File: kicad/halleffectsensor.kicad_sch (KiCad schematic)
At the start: 22 parts, among them J1 Conn_01x03, J2 Conn_01x02, Q1 2N3904, U3 ER_OLEDM0.91_1x-I2C, U5 XIAO-nRF52840-SMD

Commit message: Finished PCB and BOM
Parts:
- U2: footprint Package_SO:SOIC-8_4.4x5.0mm_P1.27mm -> Package_SO:JEITA_SOIC-8_3.9x4.9mm_P1.27mm
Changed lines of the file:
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@@
 			)
 		)
-		(property "Footprint" "Package_SO:SOIC-8_4.4x5.0mm_P1.27mm"
+		(property "Footprint" "Package_SO:JEITA_SOIC-8_3.9x4.9mm_P1.27mm"
 			(at 97.79 48.26 0)
 			(hide yes)
@@
 			)
 		)
-		(property "Footprint" "Package_SO:SOIC-8_4.4x5.0mm_P1.27mm"
+		(property "Footprint" "Package_SO:JEITA_SOIC-8_3.9x4.9mm_P1.27mm"
 			(at 52.07 85.09 0)
 			(hide yes)
@@
 			)
 		)
-		(property "Footprint" "Package_SO:SOIC-8_4.4x5.0mm_P1.27mm"
+		(property "Footprint" "Package_SO:JEITA_SOIC-8_3.9x4.9mm_P1.27mm"
 			(at 102.87 81.28 0)
 			(hide yes)

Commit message: Update pcb because github didn't work for some reason
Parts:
- removed U2: (no value), Package_SO:JEITA_SOIC-8_3.9x4.9mm_P1.27mm, symbol easyeda2kicad:HT4582ARZ
- added Q2: 2N3904, Package_TO_SOT_THT:TO-92_Inline, symbol Transistor_BJT:2N3904
- added R15, R17: 470R, Resistor_SMD:R_1206_3216Metric_Pad1.30x1.75mm_HandSolder, symbol Device:R
- added R16, R18: 910R, Resistor_SMD:R_1206_3216Metric_Pad1.30x1.75mm_HandSolder, symbol Device:R
- added U4: (no value), easyeda2kicad:SOP-14_L8.6-W3.9-P1.27-LS6.0-BL, symbol easyeda2kicad:OP_AMP_4_CH
- added VR1, VR2: (no value), easyeda2kicad:Potentiometer_3_pi, symbol easyeda2kicad:RH03ADCS3X
- R1, R2, R3, R4, R5, R6: value R -> 10k; footprint Resistor_THT:R_Axial_DIN0204_L3.6mm_D1.6mm_P7.62mm_Horizontal -> Resistor_SMD:R_1206_3216Metric_Pad1.30x1.75mm_HandSolder
- R10: value 470kR -> 10k; footprint Resistor_THT:R_Axial_DIN0204_L3.6mm_D1.6mm_P7.62mm_Horizontal -> Resistor_SMD:R_1206_3216Metric_Pad1.30x1.75mm_HandSolder
- R12: value 910R -> 10kR
- R7: value 470kR -> 10kR; footprint Resistor_THT:R_Axial_DIN0204_L3.6mm_D1.6mm_P7.62mm_Horizontal -> Resistor_SMD:R_1206_3216Metric_Pad1.30x1.75mm_HandSolder
- R8: value 4.7k -> 470R; footprint Resistor_THT:R_Axial_DIN0204_L3.6mm_D1.6mm_P7.62mm_Horizontal -> Resistor_SMD:R_1206_3216Metric_Pad1.30x1.75mm_HandSolder
- R9: value 4.7k -> 10k; footprint Resistor_THT:R_Axial_DIN0204_L3.6mm_D1.6mm_P7.62mm_Horizontal -> Resistor_SMD:R_1206_3216Metric_Pad1.30x1.75mm_HandSolder
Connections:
- net 3V3: now also Q2.3 (C); no longer U3.2 (VCC)
- net 5V: now also R10.1, U4.4 (V+); no longer R1.1
- net GND: now also R12.2, R4.2, R9.2, R16.1, R18.1, U4.11 (V-); no longer R10.2, R12.1, R2.2, R5.2
- net RAW_OUT: now also R15.2, U4.3 (+); no longer R3.1, U5.2 (D1)
- net at R5.1: now also R1.1, U4.1; no longer R3.2
- net at R6.1: now also U4.6 (-), VR1.2; no longer R11.2
- net at R6.2: now also R3.1, U4.7; no longer R4.2
- net at R2.1: now also R17.2, U4.14; no longer R1.2
- net CTRL_5V: no longer names the net of R9.1
- net CTRL_5V: now also VR2.3; no longer U5.4 (D3)
- removed net OUT: R11.1, R12.2, U5.1 (D0)
- net REF_SIG: no longer names the net of R4.1
- net REF_SIG: now also R3.2, U4.13 (-); no longer U5.3 (D2)
- net WAKEUP renamed BTN
- new net: Q2.1 (E), U3.2 (VCC)
- new net: R1.2, R2.2, U4.12 (+)
- new net: R5.2, U4.2 (-), VR1.1
- new net: R11.2, U5.4 (D3)
- new net: R10.2, VR2.1
- new net CTRL_PWR: Q1.2 (B), Q2.2 (B), R11.1, R12.1
- new net OUT_3V3: R17.1, R18.2, U5.1 (D0)
- new net RAW_OUT_3V3: R15.1, R16.2, U5.2 (D1)
- new net REF_SIG_SCALED: U4.5 (+), U5.3 (D2), VR2.2

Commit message: Worked on the code and fixed an issue with pcb
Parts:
- added R13: 910R, Resistor_SMD:R_1206_3216Metric_Pad1.30x1.75mm_HandSolder, symbol Device:R
- added R14: 10kR, Resistor_SMD:R_1206_3216Metric_Pad1.30x1.75mm_HandSolder, symbol Device:R
- R11: value 470R -> 910R
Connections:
- net CTRL_PWR: no longer Q2.2 (B)
- net GND: now also R14.2
- net at U5.11 (D10): now also R13.1
- new net CTRL_OLED: Q2.2 (B), R13.2, R14.1
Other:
- moved on the sheet: Q2, U3

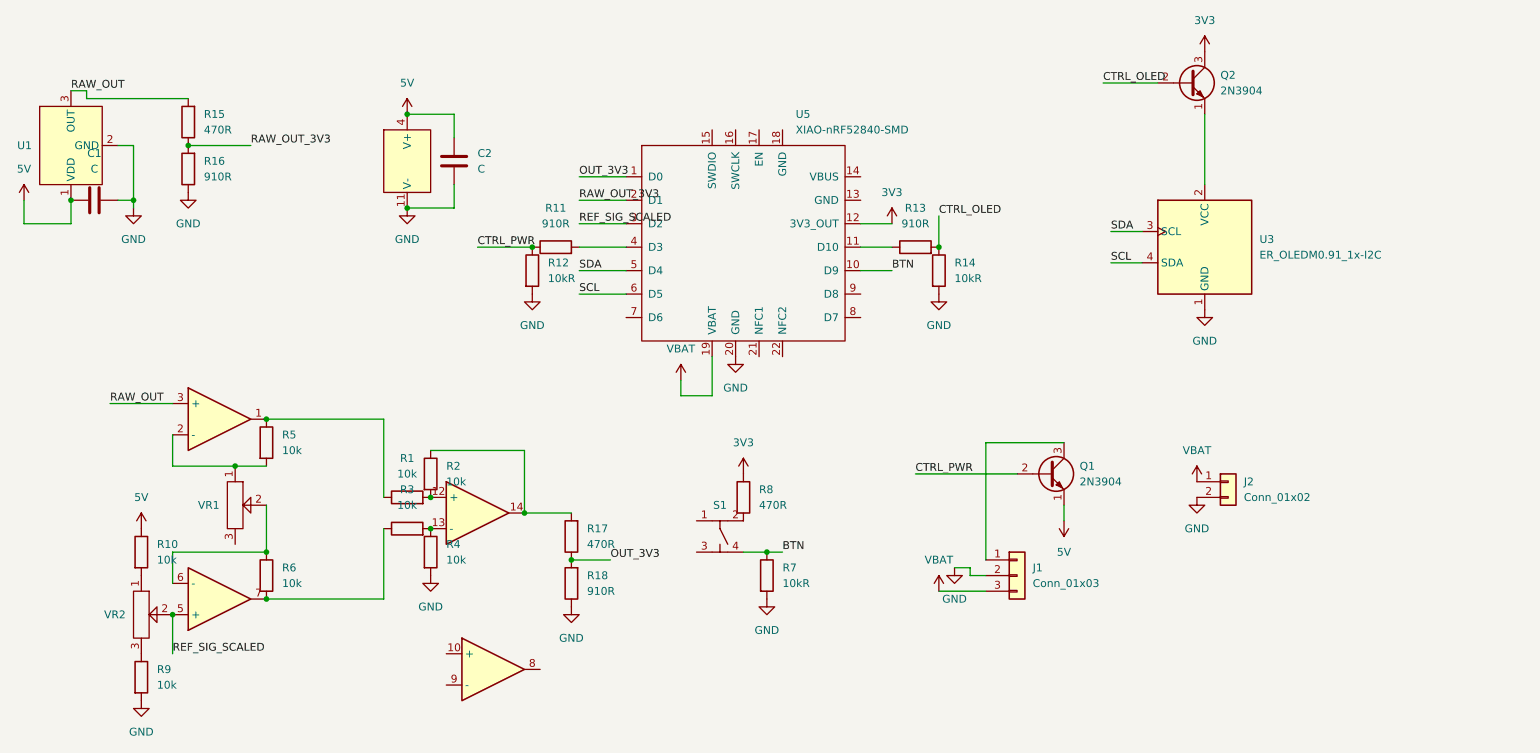
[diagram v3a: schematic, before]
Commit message: Fixed the high side mosfets
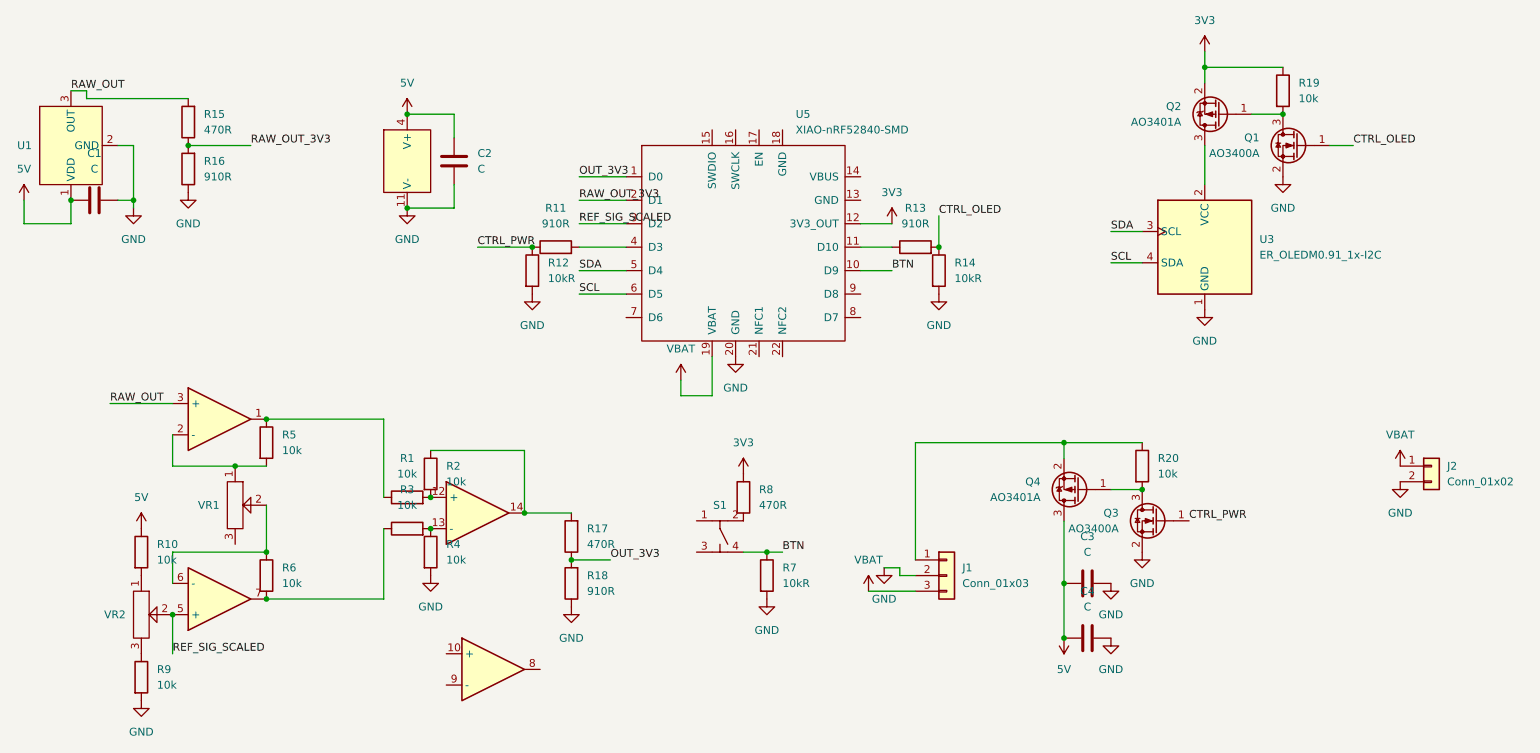
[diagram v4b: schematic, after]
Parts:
- removed Q1, Q2: 2N3904, Package_TO_SOT_THT:TO-92_Inline, symbol Transistor_BJT:2N3904
- added C3: C, Capacitor_SMD:C_1210_3225Metric_Pad1.33x2.70mm_HandSolder, symbol Device:C
- added C4: C, Capacitor_THT:C_Radial_D4.0mm_H7.0mm_P1.50mm, symbol Device:C
- added Q1, Q3: AO3400A, Package_TO_SOT_SMD:SOT-23, symbol Transistor_FET:AO3400A
- added Q2, Q4: AO3401A, Package_TO_SOT_SMD:SOT-23, symbol Transistor_FET:AO3401A
- added R19, R20: 10k, Resistor_SMD:R_1206_3216Metric_Pad1.30x1.75mm_HandSolder, symbol Device:R
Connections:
- net 3V3: now also Q2.2 (S), R19.1
- net 5V: now also C3.2, C4.2, Q4.3 (D)
- net CTRL_OLED: now also Q1.1 (G)
- net CTRL_PWR: now also Q3.1 (G)
- net GND: now also C3.1, C4.1, Q1.2 (S), Q3.2 (S)
- net at U3.2 (VCC): now also Q2.3 (D)
- net at J1.1 (Pin_1): now also Q4.2 (S), R20.1
- new net: Q1.3 (D), Q2.1 (G), R19.2
- new net: Q3.3 (D), Q4.1 (G), R20.2
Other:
- moved on the sheet: J1, J2
